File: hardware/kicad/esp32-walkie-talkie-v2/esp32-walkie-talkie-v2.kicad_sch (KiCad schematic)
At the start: 19 parts, among them J1 inmp441 left, J2 inmp441 right, J3 ST7789, J4 extend, J5 POWER_IN_5V, J6 MAX98357, J7 POWER_IN_5V, P1 Power, P2 Analog, P3 Digital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

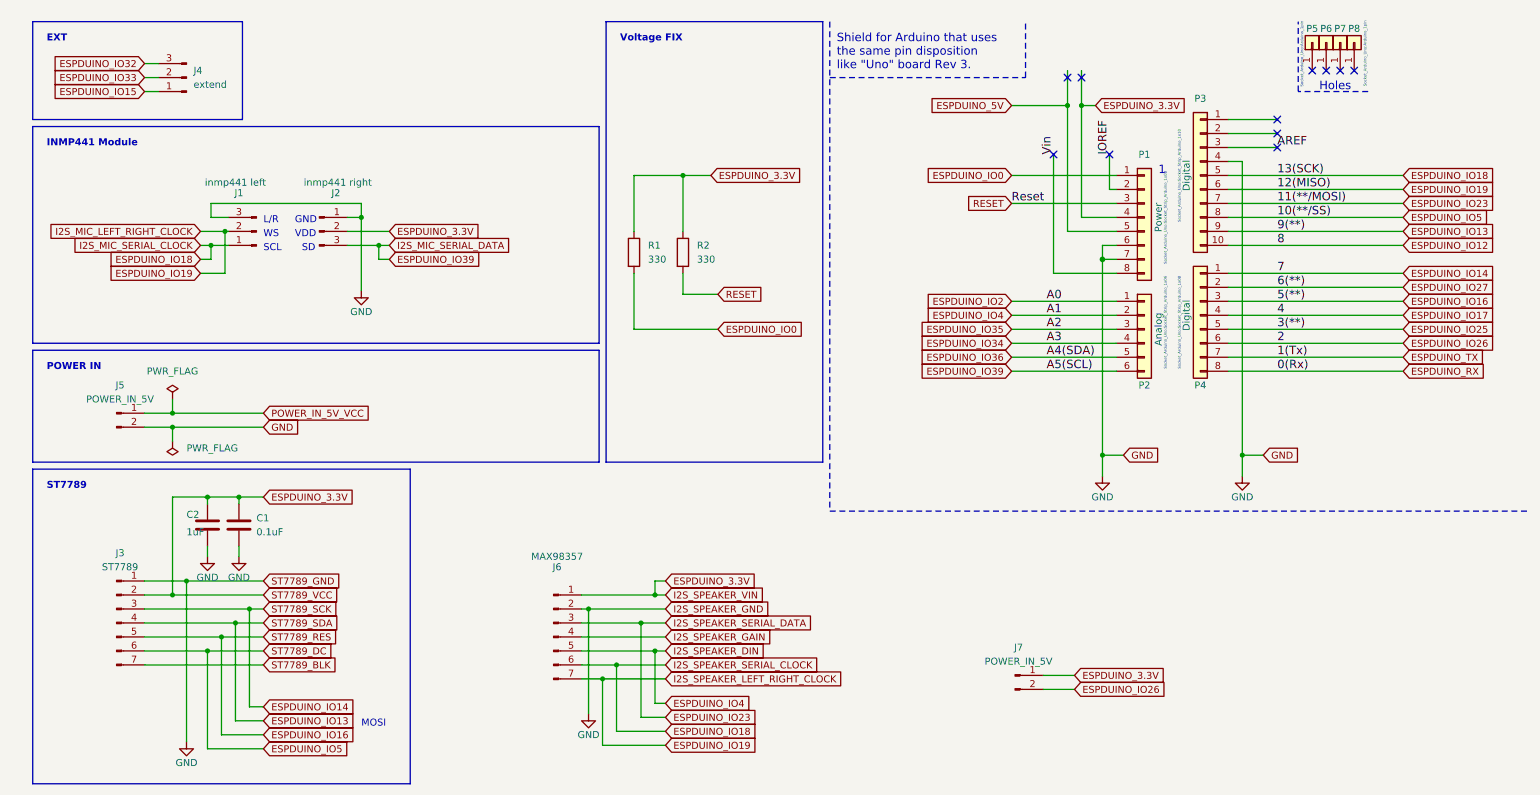
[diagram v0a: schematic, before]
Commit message: add option capacitor
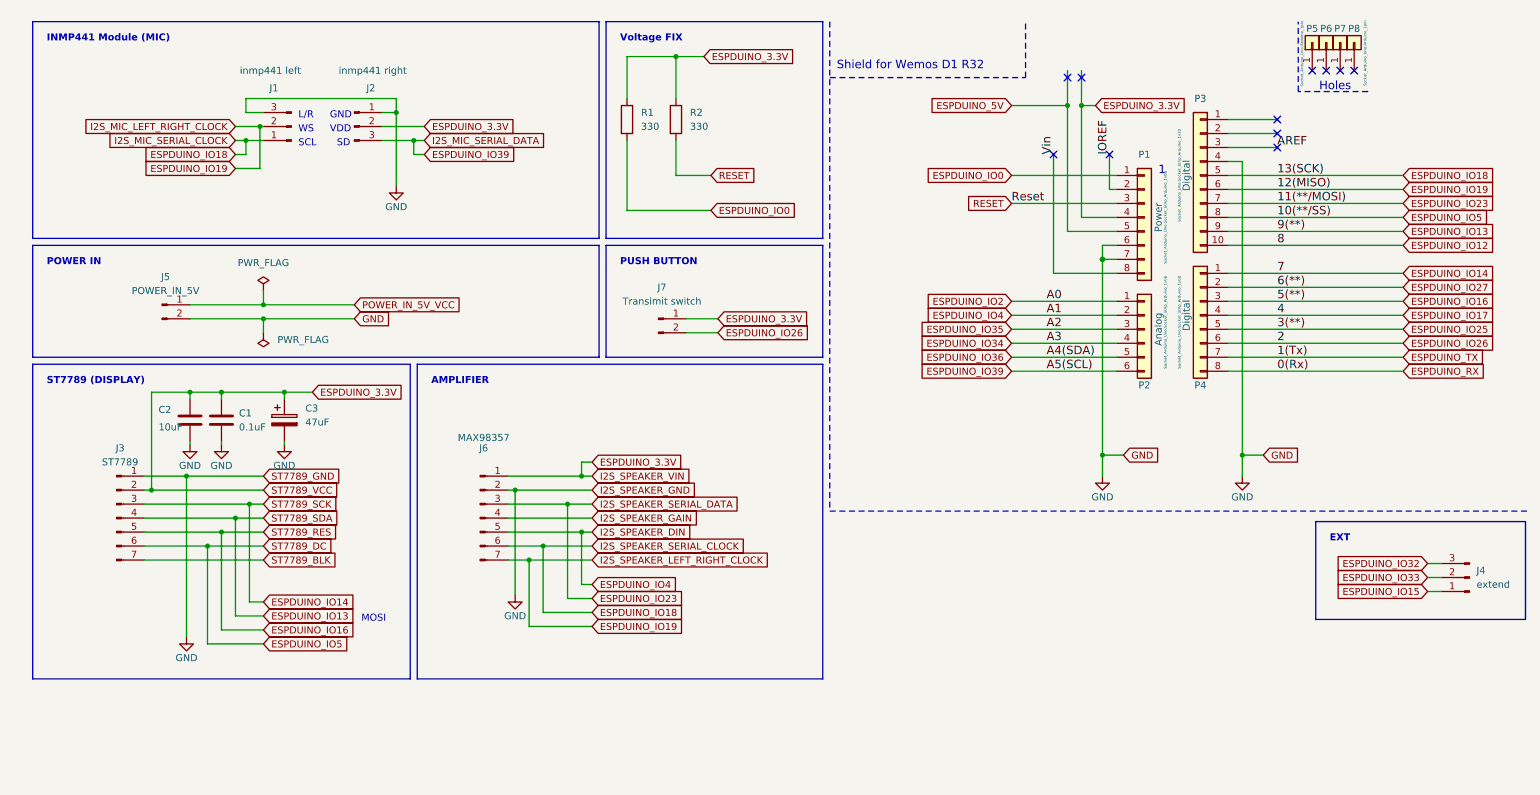
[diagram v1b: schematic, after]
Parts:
- added C3: 47uF, Capacitor_SMD:CP_Elec_6.3x5.8, symbol Device:C_Polarized
- C2: value 1uF -> 10uF; footprint Capacitor_SMD:C_0603_1608Metric -> Capacitor_Tantalum_SMD:CP_EIA-3528-12_Kemet-T
- J7: value POWER_IN_5V -> Transimit switch
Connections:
- net ESPDUINO_3.3V: now also C3.1
- net GND: now also C3.2
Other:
- note added: "AMPLIFIER"
- note added: "INMP441 Module (MIC)"
- note added: "PUSH BUTTON"
- note added: "ST7789 (DISPLAY)"
- note added: "Shield for Wemos D1 R32"
- note removed: "INMP441 Module"
- note removed: "ST7789"
- note removed: "Shield for Arduino that uses the same pin disposition like "Uno" board Rev 3."
- moved on the sheet: C1, C2, J1, J2, J3, J4, J5, J6, J7, R1, R2

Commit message: add rect capacitor option
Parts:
- added C4: 47uF, Capacitor_THT:C_Rect_L7.0mm_W2.0mm_P5.00mm, symbol Device:C_Polarized
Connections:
- net ESPDUINO_3.3V: now also C4.1
- net GND: now also C4.2
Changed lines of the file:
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@@
   (junction (at 102.87 110.49) (diameter 0) (color 0 0 0 0)
   )
+  (junction (at 54.61 66.675) (diameter 0) (color 0 0 0 0)
+  )
+  (junction (at 232.41 91.44) (diameter 0) (color 0 0 0 0)
+  )
+  (junction (at 40.64 95.25) (diameter 0) (color 0 0 0 0)
+  )
+  (junction (at 44.45 107.95) (diameter 0) (color 0 0 0 0)
+  )
+  (junction (at 81.915 34.29) (diameter 0) (color 0 0 0 0)
+  )
   (junction (at 58.42 80.01) (diameter 0) (color 0 0 0 0)
-  )
-  (junction (at 54.61 66.675) (diameter 0) (color 0 0 0 0)
-  )
-  (junction (at 232.41 91.44) (diameter 0) (color 0 0 0 0)
-  )
-  (junction (at 40.64 95.25) (diameter 0) (color 0 0 0 0)
-  )
-  (junction (at 44.45 107.95) (diameter 0) (color 0 0 0 0)
-  )
-  (junction (at 81.915 34.29) (diameter 0) (color 0 0 0 0)
   )
   (junction (at 207.01 91.44) (diameter 0) (color 0 0 0 0)
@@
     (stroke (width 0) (type default) (color 0 0 0 0))
   )
+  (wire (pts (xy 70.485 80.01) (xy 70.485 81.28))
+    (stroke (width 0) (type default) (color 0 0 0 0))
+  )
   (wire (pts (xy 52.07 118.11) (xy 54.61 118.11))
     (stroke (width 0) (type default) (color 0 0 0 0))
@@
     (stroke (width 0) (type default) (color 0 0 0 0))
   )
-  (wire (pts (xy 63.5 80.01) (xy 58.42 80.01))
-    (stroke (width 0) (type default) (color 0 0 0 0))
-  )
   (wire (pts (xy 76.2 34.29) (xy 81.915 34.29))
     (stroke (width 0) (type default) (color 0 0 0 0))
@@
     (stroke (width 0) (type default) (color 0 0 0 0))
   )
+  (wire (pts (xy 58.42 77.47) (xy 63.5 77.47))
+    (stroke (width 0) (type default) (color 0 0 0 0))
+  )
   (wire (pts (xy 44.45 125.73) (xy 54.61 125.73))
     (stroke (width 0) (type default) (color 0 0 0 0))
@@
   )
   (wire (pts (xy 54.61 64.135) (xy 71.12 64.135))
+    (stroke (width 0) (type default) (color 0 0 0 0))
+  )
+  (wire (pts (xy 70.485 88.9) (xy 70.485 89.535))
     (stroke (width 0) (type default) (color 0 0 0 0))
   )
@@
     (stroke (width 0) (type solid) (color 0 0 0 0))
   )
+  (wire (pts (xy 58.42 80.01) (xy 58.42 77.47))
+    (stroke (width 0) (type default) (color 0 0 0 0))
+  )
   (wire (pts (xy 229.87 35.56) (xy 238.76 35.56))
     (stroke (width 0) (type solid) (color 0 0 0 0))
@@
     (stroke (width 0) (type default) (color 0 0 0 0))
   )
+  (wire (pts (xy 58.42 80.01) (xy 70.485 80.01))
+    (stroke (width 0) (type default) (color 0 0 0 0))
+  )
   (wire (pts (xy 209.55 68.58) (xy 190.5 68.58))
     (stroke (width 0) (type solid) (color 0 0 0 0))
@@
     )
   )
-  (global_label "ESPDUINO_3.3V" (shape input) (at 63.5 80.01 0) (fields_autoplaced)
-    (effects (font (size 1.27 1.27)) (justify left))
-    (property "Intersheet References" "${INTERSHEET_REFS}" (id 0) (at 80.6784 79.9306 0)
+  (global_label "ESPDUINO_3.3V" (shape input) (at 63.5 77.47 0) (fields_autoplaced)
+    (effects (font (size 1.27 1.27)) (justify left))
+    (property "Intersheet References" "${INTERSHEET_REFS}" (id 0) (at 80.6784 77.3906 0)
       (effects (font (size 1.27 1.27)) (justify left) hide)
     )
@@
     (pin "1")
   )
+  (symbol (lib_id "power:GND") (at 70.485 89.535 0) (unit 1)
+    (in_bom yes) (on_board yes)
+    (property "Reference" "#PWR05" (id 0) (at 70.485 95.885 0)
+      (effects (font (size 1.27 1.27)) hide)
+    )
+    (property "Value" "GND" (id 1) (at 70.485 93.345 0))
+    (property "Footprint" "" (id 2) (at 70.485 89.535 0))
+    (property "Datasheet" "" (id 3) (at 70.485 89.535 0))
+    (pin "1")
+  )
   (symbol (lib_id "power:GND") (at 46.99 89.535 0) (unit 1)
     (in_bom yes) (on_board yes)
@@
     (pin "2")
   )
+  (symbol (lib_id "Device:C_Polarized") (at 70.485 85.09 0) (unit 1)
+    (in_bom yes) (on_board yes) (fields_autoplaced)
+    (property "Reference" "C4" (id 0) (at 74.295 82.9309 0)
+      (effects (font (size 1.27 1.27)) (justify left))
+    )
+    (property "Value" "47uF" (id 1) (at 74.295 85.4709 0)
+      (effects (font (size 1.27 1.27)) (justify left))
+    )
+    (property "Footprint" "Capacitor_THT:C_Rect_L7.0mm_W2.0mm_P5.00mm" (id 2) (at 71.4502 88.9 0)
+      (effects (font (size 1.27 1.27)) hide)
+    )
+    (property "Datasheet" "~" (id 3) (at 70.485 85.09 0)
+      (effects (font (size 1.27 1.27)) hide)
+    )
+    (pin "1")
+    (pin "2")
+  )
   (symbol (lib_id "power:GND") (at 40.64 124.46 0) (unit 1)
     (in_bom yes) (on_board yes)
@@
       (reference "#PWR04") (unit 1) (value "GND") (footprint "")
     )
+    (path "/8067f4c3-1f6c-4d7c-bd96-29bfbb5f71b2"
+      (reference "#PWR05") (unit 1) (value "GND") (footprint "")
+    )
     (path "/72427f3b-c6a8-4b37-a98a-917976f218b2"
       (reference "#PWR0101") (unit 1) (value "GND") (footprint "")
@@
       (reference "C3") (unit 1) (value "47uF") (footprint "Capacitor_SMD:CP_Elec_6.3x5.8")
     )
+    (path "/aaa61163-90e7-4d2d-a9b3-5c477d0333c8"
+      (reference "C4") (unit 1) (value "47uF") (footprint "Capacitor_THT:C_Rect_L7.0mm_W2.0mm_P5.00mm")
+    )
     (path "/9da4dd00-7568-41b6-a3c2-eaef7ee58620"

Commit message: add text, new copper fill
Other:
- note added: "WS(Word Select)"
- note added: "data come in from controller"
- note added: "data go into controller"
- note added: "pulled down by program"
- note added: "shut down mode"
- note removed: "WS"
- moved on the sheet: C4, J1, J2, J3, J6, J7

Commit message: update
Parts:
- R1, R2: footprint Resistor_SMD:R_0603_1608Metric -> Resistor_SMD:R_1206_3216Metric
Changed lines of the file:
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@@
       (effects (font (size 1.27 1.27)) (justify left))
     )
-    (property "Footprint" "Resistor_SMD:R_0603_1608Metric" (id 2) (at 127.762 30.48 90)
+    (property "Footprint" "Resistor_SMD:R_1206_3216Metric" (id 2) (at 127.762 30.48 90)
       (effects (font (size 1.27 1.27)) hide)
     )
@@
       (effects (font (size 1.27 1.27)) (justify left))
     )
-    (property "Footprint" "Resistor_SMD:R_0603_1608Metric" (id 2) (at 118.872 30.48 90)
+    (property "Footprint" "Resistor_SMD:R_1206_3216Metric" (id 2) (at 118.872 30.48 90)
       (effects (font (size 1.27 1.27)) hide)
     )
@@
     )
     (path "/f67dee4a-805c-4563-ba28-5a6bba1ad765"
-      (reference "R1") (unit 1) (value "330") (footprint "Resistor_SMD:R_0603_1608Metric")
+      (reference "R1") (unit 1) (value "330") (footprint "Resistor_SMD:R_1206_3216Metric")
     )
     (path "/5d57424f-adb7-4874-b837-6a4aae2030e9"
-      (reference "R2") (unit 1) (value "330") (footprint "Resistor_SMD:R_0603_1608Metric")
-    )
-  )
+      (reference "R2") (unit 1) (value "330") (footprint "Resistor_SMD:R_1206_3216Metric")
+    )
+  )

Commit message: update svg and pdf
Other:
- title: KEN ESP32 INTERNET RADIO HAT FOR ESPDUINO  -> ESP32 Walkie Talkie v2 
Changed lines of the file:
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@@
   (paper "A4")
   (title_block
-    (title "KEN ESP32 INTERNET RADIO HAT FOR ESPDUINO ")
-    (date "lun. 30 mars 2015")
+    (title "ESP32 Walkie Talkie v2 ")
+    (date "2022-06-21")
   )
   (junction (at 58.42 89.535) (diameter 0) (color 0 0 0 0)
